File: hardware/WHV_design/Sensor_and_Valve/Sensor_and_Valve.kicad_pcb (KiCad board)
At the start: 2 copper layers, 24.2 x 18.5 mm, 8 parts, among them J1 Conn_01x02_Pin, J2 Conn_01x02_Pin, J3 Conn_01x02_Pin, J4 Conn_01x02_Pin, Q1 NMOS, Q2 NMOS

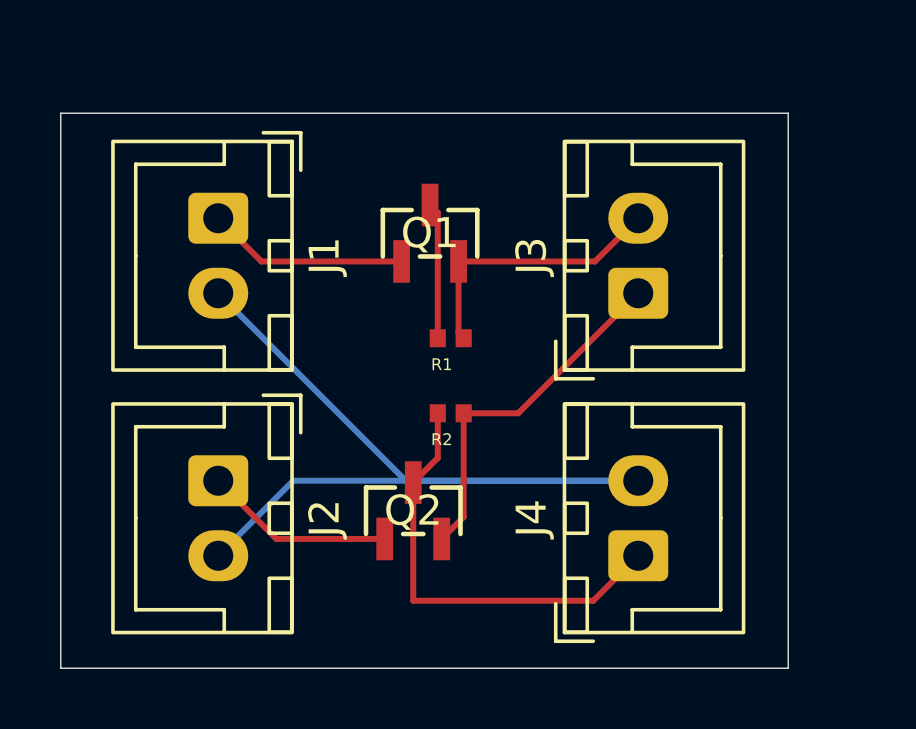
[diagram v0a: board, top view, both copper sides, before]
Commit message: Fixed footprints and redid valve pcb
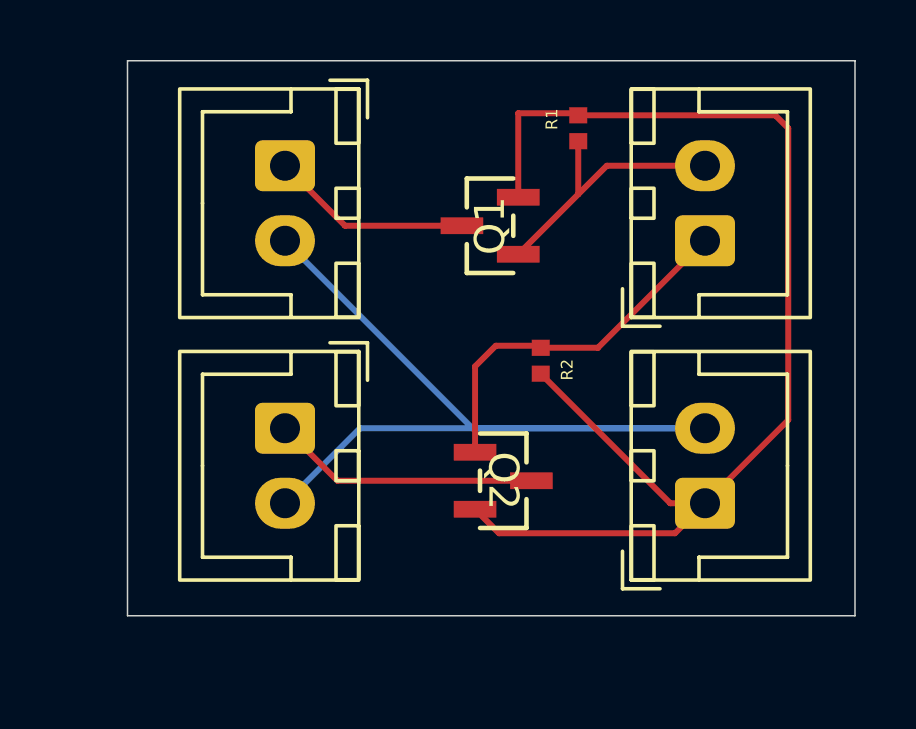
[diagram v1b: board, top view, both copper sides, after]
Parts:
- moved R1 8.19 mm to (109.5, 62.2), turned to 90 degrees
- moved R2 3.47 mm to (108.2, 70.0), turned to -90 degrees
- moved Q2 3.16 mm to (107.0, 74.0), turned to -90 degrees
- moved J1 2.83 mm to (99.7, 63.5)
- moved J2 2.83 mm to (99.7, 72.2)
- moved J3 2.83 mm to (113.7, 66.0)
- moved J4 2.83 mm to (113.7, 74.8)
- moved Q1 2.02 mm to (106.6, 65.5), turned to 90 degrees
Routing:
- net GND: track 19.3 -> 41.3 mm
- net Net-(J2-Pin_1): track 6.35 -> 8.94 mm
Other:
- board text added: "${REFERENCE}"
